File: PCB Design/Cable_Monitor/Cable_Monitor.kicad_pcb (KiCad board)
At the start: 2 copper layers, 63.5 x 118.1 mm, 59 parts, among them J1 USB_B_Mini, P1 type="R" model="Conn_01x32_Fe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, P2 type="R" model="Conn_01x32_Fe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, Q1 BSS316N, SW1 type="R" model="SW_Push" lib=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, U1 MCP6002-xSN, U2 MCP6002-xSN, U3 SiP32508, U4 LD1117S33TR_SOT223, U5 type="R" model="DRV5053_SMD" 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, U6 type="R" model="DRV5053_THT" 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, U7 MCP6002-xSN, Y1 OpenLog, Y2 Radar K-LC5-RFB-00C

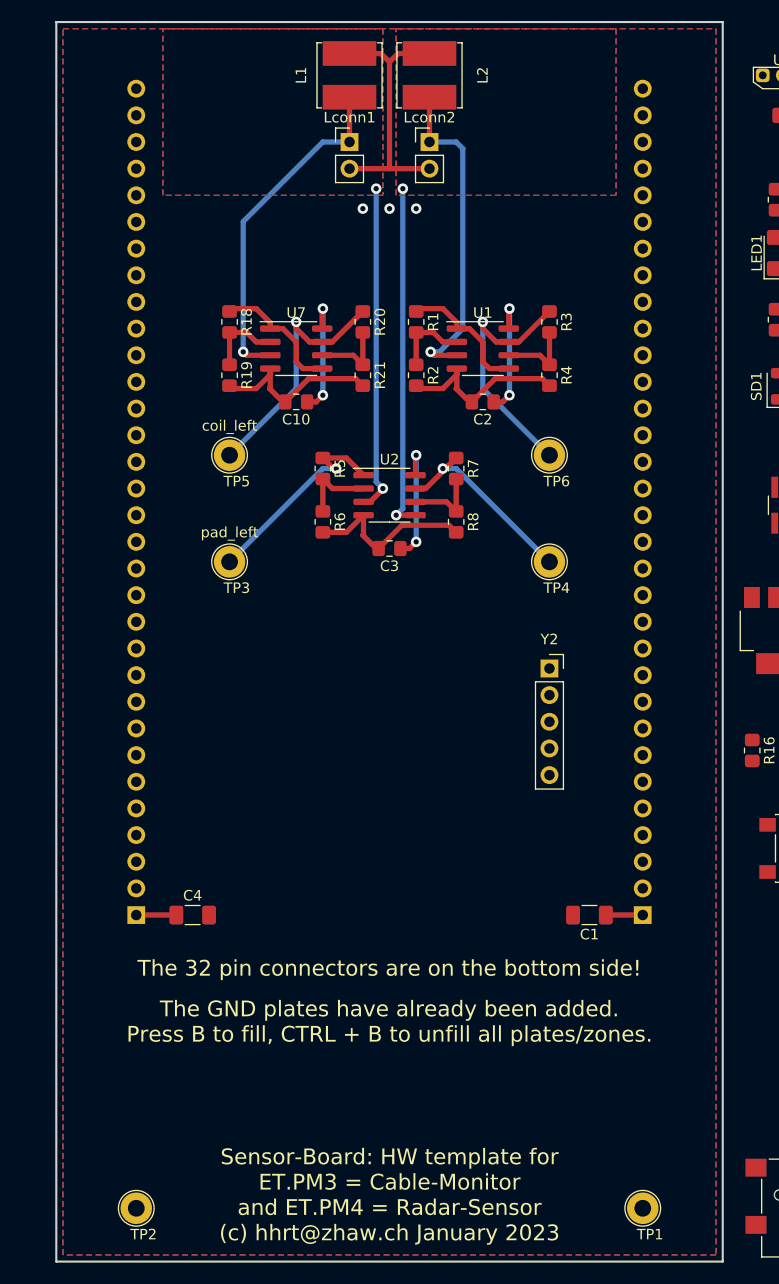
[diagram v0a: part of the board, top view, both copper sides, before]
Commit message: Modified Schematics
Added Virtual GND and adapted the Pads Left and Right
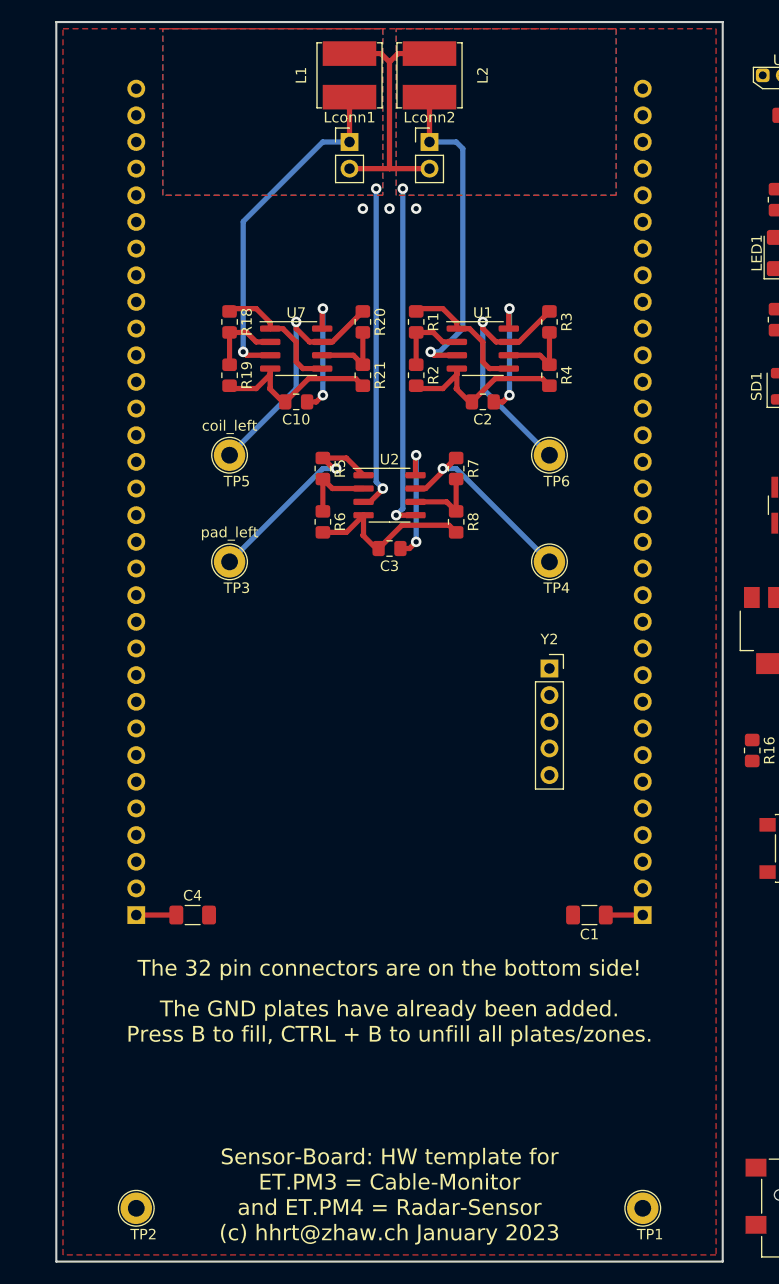
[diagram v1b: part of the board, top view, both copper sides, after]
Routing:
- removed copper zone on B.Cu, net GND
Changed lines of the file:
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@@
   (segment (start 71.055 53.34) (end 74.025 53.34) (width 0.5) (layer "F.Cu") (net 89))
   (segment (start 74.93 51.165) (end 74.93 54.245) (width 0.5) (layer "F.Cu") (net 89))
+  (zone (net 2) (net_name "GND") (layer "F.Cu") (hatch edge 0.508)
+    (connect_pads (clearance 0))
+    (min_thickness 0.127) (filled_areas_thickness no)
+    (fill (thermal_gap 0.508) (thermal_bridge_width 0.508))
+    (polygon
+      (pts
+        (xy 108.585 139.065)
+        (xy 46.355 139.065)
+        (xy 46.355 22.225)
+        (xy 108.585 22.225)
+      )
+    )
+  )
   (zone (net 63) (net_name "pad_left") (layers "F&B.Cu") (hatch edge 0.508)
     (priority 2)
     (connect_pads (clearance 0))
     (min_thickness 0.254) (filled_areas_thickness no)
-    (fill yes (thermal_gap 0.508) (thermal_bridge_width 0.508))
+    (fill (thermal_gap 0.508) (thermal_bridge_width 0.508))
     (polygon
       (pts
@@
     )
   )
-  (zone (net 2) (net_name "GND") (layers "F&B.Cu") (hatch edge 0.508)
-    (connect_pads (clearance 0))
-    (min_thickness 0.127) (filled_areas_thickness no)
-    (fill yes (thermal_gap 0.508) (thermal_bridge_width 0.508))
-    (polygon
-      (pts
-        (xy 108.585 139.065)
-        (xy 46.355 139.065)
-        (xy 46.355 22.225)
-        (xy 108.585 22.225)
-      )
-    )
-  )
   (zone (net 65) (net_name "pad_right") (layers "F&B.Cu") (hatch edge 0.508)
     (priority 2)
     (connect_pads (clearance 0))
     (min_thickness 0.254) (filled_areas_thickness no)
-    (fill yes (thermal_gap 0.508) (thermal_bridge_width 0.508))
+    (fill (thermal_gap 0.508) (thermal_bridge_width 0.508))
     (polygon
       (pts

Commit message: PCB Layout Update
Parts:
- moved TP2 133.4 mm to (160.0, 54.6), turned to 180 degrees
- moved U5 123.5 mm to (91.4, 146.3), turned to -90 degrees
- moved U6 120.5 mm to (99.7, 146.3), turned to 180 degrees
- moved C8 116.1 mm to (91.4, 142.5), turned to 0 degrees
- moved P1 114.1 mm to (160.0, 66.3), turned to 180 degrees
- moved C9 113.4 mm to (97.8, 142.5), turned to 0 degrees
- moved C4 104.1 mm to (154.6, 66.3), turned to 180 degrees
- moved R11 100.7 mm to (91.4, 134.5), turned to 90 degrees
- moved R10 98.6 mm to (95.2, 134.5), turned to 90 degrees
- moved R9 97.2 mm to (99.1, 134.5), turned to 90 degrees
- moved J1 95.9 mm to (96.5, 39.6), turned to 180 degrees
- moved LED3 90.6 mm to (91.4, 129.2), turned to -90 degrees
- moved LED2 88.4 mm to (95.2, 129.2), turned to -90 degrees
- moved LED1 87.1 mm to (99.1, 129.4), turned to -90 degrees
- moved TP1 80.7 mm to (111.8, 54.6), turned to 180 degrees
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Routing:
- net coil_left: track 32.7 -> 19.4 mm
- net pad_left: track 31.2 -> 27.8 mm, vias 2 -> 9
- net pad_right: track 33.2 -> 29.8 mm, vias 2 -> 9

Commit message: somebody
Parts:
- removed C10, C2: 100n, Capacitor_SMD:C_0805_2012Metric_Pad1.18x1.45mm_HandSolder
- removed C4: 100uF, Capacitor_SMD:C_1206_3216Metric_Pad1.33x1.80mm_HandSolder
- removed C8: 100nF, Capacitor_SMD:C_0805_2012Metric_Pad1.18x1.45mm_HandSolder
- removed J1: USB_B_Mini, Connector_USB:USB_Mini-B_Lumberg_2486_01_Horizontal
- removed L1, L2: 15mH, Inductor_SMD:L_Bourns_SRN6045TA
- removed Lconn1, Lconn2: Conn_01x02_Male, Connector_PinHeader_2.54mm:PinHeader_1x02_P2.54mm_Vertical
- removed R1, R18: 10k, Resistor_SMD:R_0805_2012Metric_Pad1.20x1.40mm_HandSolder
- removed R13, R17, R19, R2, R21, R4: 1k, Resistor_SMD:R_0805_2012Metric_Pad1.20x1.40mm_HandSolder
- removed R20: 12k, Resistor_SMD:R_0805_2012Metric_Pad1.20x1.40mm_HandSolder
- removed the TP5 at (120.7, 74.3)
- removed TP6: ~, TestPoint:TestPoint_Loop_D2.60mm_Drill1.6mm_Beaded
- removed U7: MCP6002-xSN, Package_SO:SOIC-8_3.9x4.9mm_P1.27mm
- added C16: 100nF, Capacitor_SMD:C_0805_2012Metric_Pad1.18x1.45mm_HandSolder, F.Cu at (56.0, 52.8)
- added C17: 100nF, Capacitor_SMD:C_0805_2012Metric_Pad1.18x1.45mm_HandSolder, F.Cu at (78.3, 67.7)
- added C20: 100n, Capacitor_SMD:C_0805_2012Metric_Pad1.18x1.45mm_HandSolder, F.Cu at (56.0, 71.3)
- added C5: 100nF, Capacitor_SMD:C_0805_2012Metric_Pad1.18x1.45mm_HandSolder, F.Cu at (56.0, 46.8)
- added U6: DRV5053_SMD, Package_TO_SOT_SMD:SOT-23, F.Cu at (118.4, 76.7)
- C3: value 100n -> 4.7uF; footprint Capacitor_SMD:C_0805_2012Metric_Pad1.18x1.45mm_HandSolder -> Capacitor_SMD:C_1206_3216Metric_Pad1.33x1.80mm_HandSolder
- C7: value 10uF -> 100n
- R3: value 12k -> 1M
- U1: value MCP6002-xSN -> SiP32508; footprint Package_SO:SOIC-8_3.9x4.9mm_P1.27mm -> Package_TO_SOT_SMD:TSOT-23-6_HandSoldering
- U2: value MCP6002-xSN -> LD1117S33TR; footprint Package_SO:SOIC-8_3.9x4.9mm_P1.27mm -> Package_TO_SOT_SMD:SOT-223-3_TabPin2
- U3: value SiP32508 -> MCP6002-xSN; footprint Package_TO_SOT_SMD:TSOT-23-6_HandSoldering -> Package_SO:SOIC-8_3.9x4.9mm_P1.27mm
- U4: value LD1117S33TR_SOT223 -> MCP6002-xSN; footprint Package_TO_SOT_SMD:SOT-223-3_TabPin2 -> Package_SO:SOIC-8_3.9x4.9mm_P1.27mm
- U5: value type="R" model="DRV5053_SMD" lib="" -> DRV5053_SMD
- moved U5 95.6 mm to (60.9, 55.8), turned to 0 degrees
- moved R3 90.8 mm to (60.8, 71.3), turned to 0 degrees
- moved R7 81.8 mm to (63.7, 98.4), turned to 0 degrees
- moved R8 81.2 mm to (63.7, 101.3), turned to 0 degrees
- moved U1 78.4 mm to (66.8, 55.8)
- moved U2 78.0 mm to (63.3, 49.4)
- moved C3 73.4 mm to (66.3, 59.7), turned to 0 degrees
- moved R5 68.0 mm to (63.7, 92.5), turned to 0 degrees
- moved C6 67.6 mm to (56.0, 49.8), turned to 0 degrees
- moved R6 67.5 mm to (63.7, 95.4), turned to 0 degrees
- moved C1 66.1 mm to (64.3, 106.5)
- moved U3 56.0 mm to (57.8, 66.6), turned to 0 degrees
- moved U4 28.8 mm to (70.3, 94.2), turned to 0 degrees
- moved C7 23.2 mm to (68.5, 99.0), turned to 0 degrees
- renumbered C9 to C19, R9 to R23, R10 to R24, R11 to R25, R12 to R26, R14 to R27, R15 to R28, R16 to R29, TP3 to TP4, TP4 to TP5, U6 to U8
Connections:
- C3 pad 1: +3V0 -> +5V
- C6 pad 1: Net-(U4-VI) -> +3V0
- C7 pad 1: Net-(U4-VO) -> +3V0
- R3 pad 1: PC1_ -> pad_left
- R3 pad 2: Net-(U1B--) -> VGND
- R5 pad 1: PF6 -> Net-(C10-Pad1)
- R5 pad 2: Net-(U2A--) -> Net-(U4A--)
- R6 pad 1: Net-(U2A--) -> Net-(U4A--)
- R6 pad 2: GND -> Net-(C8-Pad1)
- R7 pad 1: PC3 -> Net-(C11-Pad1)
- R7 pad 2: Net-(U2B--) -> Net-(U4B--)
- R8 pad 1: Net-(U2B--) -> Net-(U4B--)
- R8 pad 2: GND -> Net-(C9-Pad1)
- U1 pad 1: Net-(U1B-+) -> Net-(U2-VI)
- U1 pad 2: Net-(U1A--) -> Net-(U2-VI)
- U1 pad 3: coil_right -> Enable
- U1 pad 5: Net-(U1B-+) -> +5V
- U1 pad 6: Net-(U1B--) -> +5V
- U2 pad 1: PF6 -> GND
- U2 pad 2: Net-(U2A--) -> +3V0
- U2 pad 3: pad_left -> Net-(U2-VI)
- U3 pad 1: Net-(U4-VI) -> PF6
- U3 pad 2: Net-(U4-VI) -> Net-(U3A--)
- U3 pad 3: Enable -> VGND
- U3 pad 4: GND -> +3V0
- U3 pad 5: +5V -> VGND
- U3 pad 6: +5V -> Net-(U3B--)
- U4 pad 1: GND -> Net-(C10-Pad1)
- U4 pad 2: Net-(U4-VO) -> Net-(U4A--)
- U4 pad 3: Net-(U4-VI) -> pad_left
- U5 pad 2: unconnected-(U5-OUT-Pad2) -> PF8_
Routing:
- net GND: track 78.5 -> 0.00 mm, vias 3 -> 0
- net +3V0: track 39.4 -> 0.00 mm, vias 6 -> 0
- net coil_right: track 31.5 -> 0.00 mm, vias 1 -> 0
- net pad_right: track 29.8 -> 0.00 mm, vias 9 -> 8
- net pad_left: track 27.8 -> 0.00 mm, vias 9 -> 8
- net PF8_: track 24.0 -> 0.00 mm, vias 1 -> 0
- net PC1_: track 24.0 -> 0.00 mm, vias 1 -> 0
- net PC3: track 20.6 -> 0.00 mm, vias 1 -> 0
- net PF6: track 20.1 -> 0.00 mm, vias 1 -> 0
- net coil_left: track 19.4 -> 0.00 mm, vias 1 -> 0
- net Net-(U1B-+): track 12.8 -> 0.00 mm
- net Net-(U7B-+): track 12.8 -> 0.00 mm
- net Net-(U7B--): track 7.33 -> 0.00 mm
- net Net-(U7A--): track 7.33 -> 0.00 mm
- net Net-(U2B--): track 7.33 -> 0.00 mm
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
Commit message: PCB Design Update
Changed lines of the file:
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@@
         (xy 127.635 49.53)
         (xy 104.775 49.53)
-        (xy 104.775 33.655)
-        (xy 127.635 33.655)
+        (xy 104.775 33.909)
+        (xy 127.635 33.909)
       )
     )
@@
         (xy 167.005 49.53)
         (xy 144.145 49.53)
-        (xy 144.145 33.655)
-        (xy 167.005 33.655)
+        (xy 144.145 33.909)
+        (xy 167.005 33.909)
       )
     )

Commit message: Letzte Anpassungen am Schema
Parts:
- added BZ1: Buzzer, Buzzer_Beeper:Buzzer_12x9.5RM7.6, F.Cu at (180.4, 43.7)
- added C10: 100n, Capacitor_SMD:C_0805_2012Metric_Pad1.18x1.45mm_HandSolder, F.Cu at (205.0, 66.5)
- added C15: 100n, Capacitor_SMD:C_0805_2012Metric_Pad1.18x1.45mm_HandSolder, F.Cu at (209.8, 44.9)
- added C24: 100nF, Capacitor_SMD:C_0805_2012Metric_Pad1.18x1.45mm_HandSolder, F.Cu at (205.0, 55.5)
- added C25: 100nF, Capacitor_SMD:C_0805_2012Metric_Pad1.18x1.45mm_HandSolder, F.Cu at (205.0, 58.5)
- added C8: 10uF, Capacitor_SMD:C_0805_2012Metric_Pad1.18x1.45mm_HandSolder, F.Cu at (179.8, 59.9)
- added C9: 100n, Capacitor_SMD:C_0805_2012Metric_Pad1.18x1.45mm_HandSolder, F.Cu at (205.0, 63.5)
- added LED4: LEDred_3mm, LED_THT:LED_D3.0mm, F.Cu at (190.3, 53.3)
- added LED5: LEDred_3mm, LED_THT:LED_D3.0mm, F.Cu at (190.3, 58.8)
- added Lconn1: Conn_01x02_Male, Connector_PinHeader_2.54mm:PinHeader_1x02_P2.54mm_Vertical, F.Cu at (193.3, 39.3)
- added Lconn2: Conn_01x02_Male, Connector_PinHeader_2.54mm:PinHeader_1x02_P2.54mm_Vertical, F.Cu at (198.0, 39.3)
- added Q2: BSS316N, Package_TO_SOT_SMD:SOT-23, F.Cu at (198.2, 46.4)
- added R15: 1M, Resistor_SMD:R_0805_2012Metric_Pad1.20x1.40mm_HandSolder, F.Cu at (205.0, 38.4)
- added R16: 1k, Resistor_SMD:R_0805_2012Metric_Pad1.20x1.40mm_HandSolder, F.Cu at (205.0, 41.4)
- added R17: 1M, Resistor_SMD:R_0805_2012Metric_Pad1.20x1.40mm_HandSolder, F.Cu at (205.0, 44.3)
- added R18: 1k, Resistor_SMD:R_0805_2012Metric_Pad1.20x1.40mm_HandSolder, F.Cu at (205.0, 47.3)
- added R21: 65, Resistor_SMD:R_0805_2012Metric_Pad1.20x1.40mm_HandSolder, F.Cu at (209.8, 55.5)
- added R22: 47, Resistor_SMD:R_0805_2012Metric_Pad1.20x1.40mm_HandSolder, F.Cu at (209.8, 58.4)
- added R30: 62, Resistor_SMD:R_0805_2012Metric_Pad1.20x1.40mm_HandSolder, F.Cu at (193.4, 45.6)
- added R31: 62, Resistor_SMD:R_0805_2012Metric_Pad1.20x1.40mm_HandSolder, F.Cu at (193.4, 48.6)
- added R4: 1M, Resistor_SMD:R_0805_2012Metric_Pad1.20x1.40mm_HandSolder, F.Cu at (205.0, 69.5)
- added SW2: type="R" model="SW_Push" lib="", Button_Switch_SMD:SW_SPST_PTS645, F.Cu at (183.0, 54.4)
- added TP6: HS_left, TestPoint:TestPoint_Loop_D2.60mm_Drill1.6mm_Beaded, F.Cu at (197.0, 53.0)
- added TP7: HS_right, TestPoint:TestPoint_Loop_D2.60mm_Drill1.6mm_Beaded, F.Cu at (197.0, 58.1)
- added U7: MCP6002-xSN, Package_SO:SOIC-8_3.9x4.9mm_P1.27mm, F.Cu at (211.6, 40.2)
- added U9: type="R" model="DRV5053_THT" lib="", HW_template:TO-92Flat_wide, F.Cu at (204.7, 52.2)
- C6: value 10uF -> 100nF
- C7: value 100n -> 100nF
- R23: value 22 -> 100
- R24: value 47 -> 100
- R26: value 100 -> 100k
- R27: value 100 -> 10
- U2: value LD1117S33TR -> DRV5053_THT; footprint Package_TO_SOT_SMD:SOT-223-3_TabPin2 -> HW_template:TO-92Flat_wide
- U3: value MCP6002-xSN -> DRV5053_THT; footprint Package_SO:SOIC-8_3.9x4.9mm_P1.27mm -> HW_template:TO-92Flat_wide
- U4: value MCP6002-xSN -> LD1117S33TR; footprint Package_SO:SOIC-8_3.9x4.9mm_P1.27mm -> Package_TO_SOT_SMD:SOT-223-3_TabPin2
- U5, U6: value DRV5053_SMD -> MCP6002-xSN; footprint Package_TO_SOT_SMD:SOT-23 -> Package_SO:SOIC-8_3.9x4.9mm_P1.27mm
- U8: value type="R" model="DRV5053_THT" lib="" -> type="R" model="DRV5053_SMD" lib=""; footprint HW_template:TO-92Flat_wide -> Package_TO_SOT_SMD:SOT-23
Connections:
- C5 pad 1: Net-(U2-VI) -> GND
- C5 pad 2: GND -> +3V0
- C6 pad 1: +3V0 -> GND
- C6 pad 2: GND -> +3V0
- C7 pad 1: +3V0 -> Net-(U4-VI)
- R23 pad 2: Net-(LED1-A) -> Net-(LED3-A)
- R24 pad 2: Net-(LED2-A) -> Net-(SD1-A)
- R25 pad 2: Net-(LED3-A) -> Net-(SD2-A)
- R26 pad 2: Net-(SD1-A) -> GND
- R27 pad 1: Enable -> +5V
- R27 pad 2: Net-(SD2-A) -> Net-(Q1-D)
- R28 pad 1: Enable -> PA5
- U1 pad 1: Net-(U2-VI) -> Net-(U4-VI)
- U1 pad 2: Net-(U2-VI) -> Net-(U4-VI)
- U2 pad 1: GND -> +3V0
- U2 pad 2: +3V0 -> GND
- U2 pad 3: Net-(U2-VI) -> HS_left
- U3 pad 1: PF6 -> +3V0
- U3 pad 2: Net-(U3A--) -> GND
- U3 pad 3: VGND -> HS_right
- U4 pad 1: Net-(C10-Pad1) -> GND
- U4 pad 2: Net-(U4A--) -> +3V0
- U4 pad 3: pad_left -> Net-(U4-VI)
- U5 pad 1: +3V0 -> Net-(U5A--)
- U5 pad 2: PF8_ -> Net-(U5A--)
- U5 pad 3: GND -> pad_left
- U6 pad 1: +3V0 -> Net-(U6A--)
- U6 pad 2: PC1_ -> Net-(U6A--)
- U6 pad 3: GND -> pad_right
- U8 pad 2: GND -> unconnected-(U8-OUT-Pad2)
- U8 pad 3: unconnected-(U8-OUT-Pad3) -> GND

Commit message: Schema Updates, bald Fertig
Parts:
- removed C24, C25: 100nF, Capacitor_SMD:C_0805_2012Metric_Pad1.18x1.45mm_HandSolder
- removed LED3: LEDred, LED_SMD:LED_1206_3216Metric_Pad1.42x1.75mm_HandSolder
- removed LED4, LED5: LEDred_3mm, LED_THT:LED_D3.0mm
- removed Q2: BSS316N, Package_TO_SOT_SMD:SOT-23
- removed R24, R25: 100, Resistor_SMD:R_0805_2012Metric_Pad1.20x1.40mm_HandSolder
- removed R26, R28: 100k, Resistor_SMD:R_0805_2012Metric_Pad1.20x1.40mm_HandSolder
- removed R27, R29: 10, Resistor_SMD:R_0805_2012Metric_Pad1.20x1.40mm_HandSolder
- removed R30, R31: 62, Resistor_SMD:R_0805_2012Metric_Pad1.20x1.40mm_HandSolder
- removed SD1: SD103AWS, Diode_SMD:D_SOD-323_HandSoldering
- removed SD2: SS13L, Diode_SMD:D_SMA
- removed SW2: type="R" model="SW_Push" lib="", Button_Switch_SMD:SW_SPST_PTS645
- removed U8: type="R" model="DRV5053_SMD" lib="", Package_TO_SOT_SMD:SOT-23
- removed U9: type="R" model="DRV5053_THT" lib="", HW_template:TO-92Flat_wide
- removed Y1: OpenLog, Connector_PinHeader_2.54mm:PinHeader_1x06_P2.54mm_Vertical
- removed Y2: Radar K-LC5-RFB-00C, HW_template:Radar_K-LC5
- added C11: 18nF, Capacitor_SMD:C_0805_2012Metric_Pad1.18x1.45mm_HandSolder, F.Cu at (62.4, 153.5)
- added C12: 330nF, Capacitor_SMD:C_0805_2012Metric_Pad1.18x1.45mm_HandSolder, F.Cu at (62.4, 156.5)
- added C13: 18nF, Capacitor_SMD:C_0805_2012Metric_Pad1.18x1.45mm_HandSolder, F.Cu at (62.4, 159.5)
- added C14: 330nF, Capacitor_SMD:C_0805_2012Metric_Pad1.18x1.45mm_HandSolder, F.Cu at (62.4, 162.5)
- added C18: 10uF, Capacitor_SMD:C_0805_2012Metric_Pad1.18x1.45mm_HandSolder, F.Cu at (74.3, 153.5)
- added C2: 1nF, Capacitor_SMD:C_0805_2012Metric_Pad1.18x1.45mm_HandSolder, F.Cu at (67.5, 144.3)
- added C21: 10uF, Capacitor_SMD:C_0805_2012Metric_Pad1.18x1.45mm_HandSolder, F.Cu at (74.3, 156.5)
- added C22: 0.16uF, Capacitor_SMD:C_0805_2012Metric_Pad1.18x1.45mm_HandSolder, F.Cu at (74.3, 159.5)
- added C23: 0.16uF, Capacitor_SMD:C_0805_2012Metric_Pad1.18x1.45mm_HandSolder, F.Cu at (74.3, 162.5)
- added C4: 100uF, Capacitor_SMD:C_0805_2012Metric_Pad1.18x1.45mm_HandSolder, F.Cu at (67.5, 147.3)
- added J1: USB_B_Micro, Connector_USB:USB_Micro-B_Molex_47346-0001, F.Cu at (135.6, 148.6)
- added R1: 10k, Resistor_SMD:R_0805_2012Metric_Pad1.20x1.40mm_HandSolder, F.Cu at (72.3, 144.3)
- added R10: 7.5k, Resistor_SMD:R_0805_2012Metric_Pad1.20x1.40mm_HandSolder, F.Cu at (57.7, 156.4)
- added R11: 7.5k, Resistor_SMD:R_0805_2012Metric_Pad1.20x1.40mm_HandSolder, F.Cu at (57.7, 159.3)
- added R12: 560k, Resistor_SMD:R_0805_2012Metric_Pad1.20x1.40mm_HandSolder, F.Cu at (57.7, 162.3)
- added R13: 560k, Resistor_SMD:R_0805_2012Metric_Pad1.20x1.40mm_HandSolder, F.Cu at (57.7, 165.2)
- added R14: 10k, Resistor_SMD:R_0805_2012Metric_Pad1.20x1.40mm_HandSolder, F.Cu at (79.1, 153.4)
- added R19: 1k, Resistor_SMD:R_0805_2012Metric_Pad1.20x1.40mm_HandSolder, F.Cu at (79.1, 156.4)
- added R2: 10k, Resistor_SMD:R_0805_2012Metric_Pad1.20x1.40mm_HandSolder, F.Cu at (72.3, 147.2)
- added R20: 1M, Resistor_SMD:R_0805_2012Metric_Pad1.20x1.40mm_HandSolder, F.Cu at (79.1, 159.3)
- added R9: 5.1k, Resistor_SMD:R_0805_2012Metric_Pad1.20x1.40mm_HandSolder, F.Cu at (57.7, 153.4)
- added TP10: pad_left_in, TestPoint:TestPoint_Loop_D2.60mm_Drill1.6mm_Beaded, F.Cu at (62.9, 140.3)
- added TP11: 5V, TestPoint:TestPoint_Loop_D2.60mm_Drill1.6mm_Beaded, F.Cu at (67.9, 135.2)
- added TP12: pad_left_out, TestPoint:TestPoint_Loop_D2.60mm_Drill1.6mm_Beaded, F.Cu at (67.9, 140.3)
- added TP13: pad_right_out, TestPoint:TestPoint_Loop_D2.60mm_Drill1.6mm_Beaded, F.Cu at (73.0, 135.2)
- added TP14: 3V, TestPoint:TestPoint_Loop_D2.60mm_Drill1.6mm_Beaded, F.Cu at (73.0, 140.3)
- added TP15: HS_left_in, TestPoint:TestPoint_Loop_D2.60mm_Drill1.6mm_Beaded, F.Cu at (67.4, 154.5)
- added TP16: HS_right_in, TestPoint:TestPoint_Loop_D2.60mm_Drill1.6mm_Beaded, F.Cu at (67.4, 159.5)
- added TP17: HS_left_out, TestPoint:TestPoint_Loop_D2.60mm_Drill1.6mm_Beaded, F.Cu at (152.4, 162.7)
- added TP18: HS_right_out, TestPoint:TestPoint_Loop_D2.60mm_Drill1.6mm_Beaded, F.Cu at (152.4, 167.7)
- added TP19: pad_left_sf, TestPoint:TestPoint_Loop_D2.60mm_Drill1.6mm_Beaded, F.Cu at (152.4, 172.8)
- added TP20: pad_right_sf, TestPoint:TestPoint_Loop_D2.60mm_Drill1.6mm_Beaded, F.Cu at (152.4, 177.8)
- added TP21: HS_left_VGND, TestPoint:TestPoint_Loop_D2.60mm_Drill1.6mm_Beaded, F.Cu at (86.4, 137.2)
- added TP22: HS_right_VGND, TestPoint:TestPoint_Loop_D2.60mm_Drill1.6mm_Beaded, F.Cu at (86.4, 142.2)
- added TP3: GND, TestPoint:TestPoint_Loop_D2.60mm_Drill1.6mm_Beaded, F.Cu at (45.7, 129.5)
- added TP8: Virtual Ground TP, TestPoint:TestPoint_Loop_D2.60mm_Drill1.6mm_Beaded, F.Cu at (57.8, 140.3)
- added TP9: pad_left_in, TestPoint:TestPoint_Loop_D2.60mm_Drill1.6mm_Beaded, F.Cu at (62.9, 135.2)
- C16, C17: value 100nF -> 0.16uF
- C19, C6: value 100nF -> 10uF
- C20: value 100n -> 10uF
- C8: value 10uF -> 100nF
- LED1: value LEDblue -> LEDred_3mm; footprint LED_SMD:LED_1206_3216Metric_Pad1.42x1.75mm_HandSolder -> LED_THT:LED_D3.0mm
- LED2: value LEDgreen -> LEDred_3mm; footprint LED_SMD:LED_1206_3216Metric_Pad1.42x1.75mm_HandSolder -> LED_THT:LED_D3.0mm
- R15: value 1M -> 10k
- R16: value 1k -> 100k
- R17, R3: value 1M -> 100k
- R18, R6: value 1k -> 1M
- R21: value 65 -> 1k
- R22: value 47 -> 10k
- R23: value 100 -> 10k
- R4: value 1M -> 62
- R5: value 220k -> 62
- R7: value 100k -> 1M
- R8: value 1k -> 5.1k
- TP1, TP2, TP5: value ~ -> GND
- TP4: value pad_left -> GND
- TP6: value HS_left -> GND
- TP7: value HS_right -> PWM_Buzzer
- U2: value DRV5053_THT -> LD1117S33TR; footprint HW_template:TO-92Flat_wide -> Package_TO_SOT_SMD:SOT-223-3_TabPin2
- U4: value LD1117S33TR -> DRV5053_THT; footprint Package_TO_SOT_SMD:SOT-223-3_TabPin2 -> HW_template:TO-92Flat_wide
- moved U4 86.7 mm to (140.3, 43.2), turned to 90 degrees
- moved U3 78.0 mm to (131.4, 40.6), turned to -90 degrees
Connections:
- C16 pad 2: +3V0 -> Net-(C16-Pad2)
- C17 pad 2: +3V0 -> Net-(C17-Pad2)
- C19 pad 1: GND -> Net-(C17-Pad2)
- C19 pad 2: +3V0 -> Net-(U7B-+)
- C20 pad 1: +3V0 -> Net-(C20-Pad1)
- C5 pad 1: GND -> Net-(U2-VI)
- C5 pad 2: +3V0 -> GND
- C6 pad 1: GND -> +3V0
- C6 pad 2: +3V0 -> GND
- C7 pad 1: Net-(U4-VI) -> GND
- C7 pad 2: GND -> +3V0
- C8 pad 1: +3V0 -> GND
- C8 pad 2: GND -> +3V0
- Lconn1 pad 1: HS_left -> /hall-sensor_left_right/in_left
- Lconn2 pad 1: HS_right -> /hall-sensor_left_right/in_right
- Q1 pad 1: Enable -> PA5
- Q1 pad 3: Net-(Q1-D) -> Net-(BZ1-+)
- R15 pad 1: Net-(R15-Pad1) -> /hall-sensor_left_right/in_right
- R15 pad 2: Net-(U7A--) -> Net-(C17-Pad2)
- R16 pad 1: Net-(U7A--) -> Net-(U7A-+)
- R16 pad 2: Net-(C20-Pad1) -> VGND
- R17 pad 1: Net-(R17-Pad1) -> Net-(U7B-+)
- R17 pad 2: Net-(U7B--) -> VGND
- R18 pad 1: Net-(U7B--) -> Net-(R18-Pad1)
- R18 pad 2: Net-(C21-Pad1) -> Net-(U7A--)
- R21 pad 1: Enable -> Net-(U7B--)
- R21 pad 2: Net-(LED1-A) -> Net-(C21-Pad1)
- R22 pad 1: Enable -> Net-(R18-Pad1)
- R22 pad 2: Net-(LED2-A) -> PF8_
- R23 pad 1: Enable -> Net-(R20-Pad1)
- R23 pad 2: Net-(LED3-A) -> PC1_
- R3 pad 1: pad_left -> PA5
- R3 pad 2: VGND -> GND
- R4 pad 1: pad_left -> PE15_
- R4 pad 2: VGND -> Net-(LED1-A)
- R5 pad 1: Net-(C10-Pad1) -> PE13_
- R5 pad 2: Net-(U4A--) -> Net-(LED2-A)
- R6 pad 1: Net-(U4A--) -> pad_right
- R6 pad 2: Net-(C8-Pad1) -> VGND
- R7 pad 1: Net-(C11-Pad1) -> pad_left
- R7 pad 2: Net-(U4B--) -> VGND
- R8 pad 1: Net-(U4B--) -> Net-(U6A--)
- TP4 pad 1: PF6 -> GND
- TP5 pad 1: PC3 -> GND
- TP6 pad 1: PF8_ -> GND
- TP7 pad 1: PC1_ -> PA5
- U1 pad 1: Net-(U4-VI) -> Net-(U2-VI)
- U1 pad 2: Net-(U4-VI) -> Net-(U2-VI)
- U2 pad 1: +3V0 -> GND
- U2 pad 2: GND -> +3V0
- U2 pad 3: HS_left -> Net-(U2-VI)
- U3 pad 3: HS_right -> /hall-sensor_left_right/in_left
- U4 pad 1: GND -> +3V0
- U4 pad 2: +3V0 -> GND
- U4 pad 3: Net-(U4-VI) -> /hall-sensor_left_right/in_right
- U7 pad 1: Net-(R15-Pad1) -> Net-(R18-Pad1)
- U7 pad 7: Net-(R17-Pad1) -> Net-(R20-Pad1)
